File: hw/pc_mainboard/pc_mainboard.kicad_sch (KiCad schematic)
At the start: 0 parts

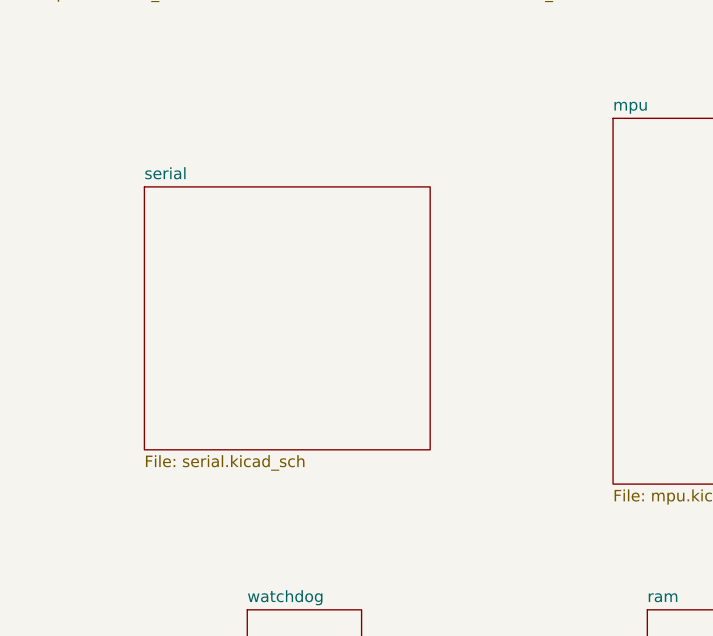
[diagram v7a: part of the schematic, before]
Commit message: SD card research, updated some formatting (#49)
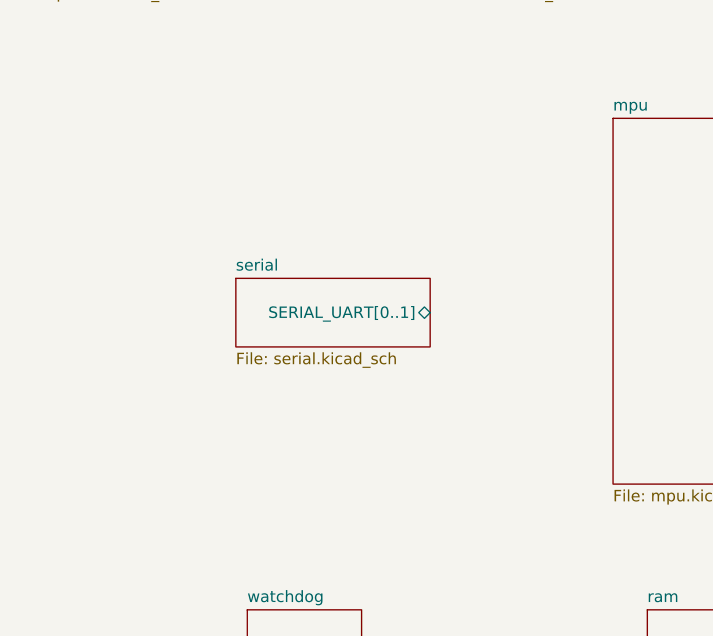
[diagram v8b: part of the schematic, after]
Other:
- sheet serial ports: added SERIAL_UART[0..1]; removed none
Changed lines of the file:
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@@
 	)
 	(sheet
-		(at 193.04 177.8)
-		(size 31.75 29.21)
+		(at 203.2 187.96)
+		(size 21.59 7.62)
 		(exclude_from_sim no)
 		(in_bom yes)
@@
 		)
 		(property "Sheetname" "serial"
-			(at 193.04 177.0884 0)
+			(at 203.2 187.2484 0)
 			(effects
 				(font
@@
 		)
 		(property "Sheetfile" "serial.kicad_sch"
-			(at 193.04 207.5946 0)
+			(at 203.2 196.1646 0)
 			(effects
 				(font
@@
 			)
 		)
+		(pin "SERIAL_UART[0..1]" bidirectional
+			(at 224.79 191.77 0)
+			(effects
+				(font
+					(size 1.27 1.27)
+				)
+				(justify right)
+			)
+		)
